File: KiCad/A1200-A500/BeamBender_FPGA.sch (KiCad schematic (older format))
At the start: 1 part, among them U2 GW1NR-UV9LQ144P

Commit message: more routing done
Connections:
- net B0_FPGA: now also U2.40 (IOB9A)
- net B1_FPGA: now also U2.41 (IOB9B)
- net B2_FPGA: now also U2.42 (IOB11A)
- net B3_FPGA: now also U2.43 (IOB11B)
- net B4_FPGA: now also U2.44 (IOB12A)
- net B5_FPGA: now also U2.45 (IOB12B)
- net B6_FPGA: now also U2.46 (IOB13A)
- net B7_FPGA: now also U2.47 (IOB13B)
- net G0_FPGA: now also U2.48 (IOB15A); no longer U2.47 (IOB13B)
- net PCLK: now also U2.34 (IOB6B); no longer U2.48 (IOB15A)
- net VSYNC_FPGA: now reaches U2.32 (IOB6A)
- net HSYNC_FPGA: now reaches U2.38 (IOB8A)
- net DE: now reaches U2.39 (IOB8B)
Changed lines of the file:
@@
 Text GLabel 6500 1800 2    50   Input ~ 0
 GCLKT_1
-Text GLabel 3050 6150 3    50   Output ~ 0
+Text GLabel 1600 5400 0    50   Output ~ 0
 PCLK
 Text GLabel 1600 3000 0    50   Input ~ 0
@@
 Text GLabel 6500 3950 2    50   Input ~ 0
 C14M_3V3
-Text GLabel 8050 4950 2    50   Input ~ 0
+Text GLabel 2250 6150 3    50   Output ~ 0
 B0_FPGA
-Text GLabel 8050 4850 2    50   Input ~ 0
+Text GLabel 2350 6150 3    50   Output ~ 0
 B1_FPGA
-Text GLabel 8050 4750 2    50   Input ~ 0
+Text GLabel 2450 6150 3    50   Output ~ 0
 B2_FPGA
-Text GLabel 8050 4650 2    50   Input ~ 0
+Text GLabel 2550 6150 3    50   Output ~ 0
 B3_FPGA
-Text GLabel 8050 4550 2    50   Input ~ 0
+Text GLabel 2650 6150 3    50   Output ~ 0
 B4_FPGA
-Text GLabel 8050 4450 2    50   Input ~ 0
+Text GLabel 2750 6150 3    50   Output ~ 0
 B5_FPGA
-Text GLabel 8050 4350 2    50   Input ~ 0
+Text GLabel 2850 6150 3    50   Output ~ 0
 B6_FPGA
-Text GLabel 8050 4250 2    50   Input ~ 0
+Text GLabel 2950 6150 3    50   Output ~ 0
 B7_FPGA
-Text GLabel 2950 6150 3    50   Input ~ 0
+Text GLabel 3050 6150 3    50   Output ~ 0
 G0_FPGA
-Text GLabel 3150 6150 3    50   Input ~ 0
+Text GLabel 3150 6150 3    50   Output ~ 0
 G1_FPGA
-Text GLabel 3250 6150 3    50   Input ~ 0
+Text GLabel 3250 6150 3    50   Output ~ 0
 G2_FPGA
-Text GLabel 3350 6150 3    50   Input ~ 0
+Text GLabel 3350 6150 3    50   Output ~ 0
 G3_FPGA
-Text GLabel 3450 6150 3    50   Input ~ 0
+Text GLabel 3450 6150 3    50   Output ~ 0
 G4_FPGA
-Text GLabel 3600 6150 3    50   Input ~ 0
+Text GLabel 3600 6150 3    50   Output ~ 0
 G5_FPGA
-Text GLabel 3750 6150 3    50   Input ~ 0
+Text GLabel 3750 6150 3    50   Output ~ 0
 G6_FPGA
-Text GLabel 3850 6150 3    50   Input ~ 0
+Text GLabel 3850 6150 3    50   Output ~ 0
 G7_FPGA
-Text GLabel 4050 6150 3    50   Input ~ 0
+Text GLabel 4050 6150 3    50   Output ~ 0
 R0_FPGA
-Text GLabel 4150 6150 3    50   Input ~ 0
+Text GLabel 4150 6150 3    50   Output ~ 0
 R1_FPGA
-Text GLabel 4250 6150 3    50   Input ~ 0
+Text GLabel 4250 6150 3    50   Output ~ 0
 R2_FPGA
-Text GLabel 4350 6150 3    50   Input ~ 0
+Text GLabel 4350 6150 3    50   Output ~ 0
 R3_FPGA
-Text GLabel 4450 6150 3    50   Input ~ 0
+Text GLabel 4450 6150 3    50   Output ~ 0
 R4_FPGA
-Text GLabel 4550 6150 3    50   Input ~ 0
+Text GLabel 4550 6150 3    50   Output ~ 0
 R5_FPGA
-Text GLabel 4650 6150 3    50   Input ~ 0
+Text GLabel 4650 6150 3    50   Output ~ 0
 R6_FPGA
-Text GLabel 4750 6150 3    50   Input ~ 0
+Text GLabel 4750 6150 3    50   Output ~ 0
 R7_FPGA
-Text GLabel 5150 6150 3    50   Input ~ 0
-R0_3V3
-Text GLabel 5250 6150 3    50   Input ~ 0
-R1_3V3
-Text GLabel 5350 6150 3    50   Input ~ 0
-R2_3V3
-Text GLabel 5450 6150 3    50   Input ~ 0
-R3_3V3
 Text GLabel 6500 4650 2    50   Input ~ 0
 B0_3V3
@@
 Text GLabel 6500 4850 2    50   Input ~ 0
 G7_3V3
-Text GLabel 5550 6150 3    50   Input ~ 0
-R4_3V3
-Text GLabel 5650 6150 3    50   Input ~ 0
-R5_3V3
-Text GLabel 6500 5750 2    50   Input ~ 0
-R6_3V3
 Text GLabel 6500 5650 2    50   Input ~ 0
 R7_3V3
 Text GLabel 3950 6150 3    50   Input ~ 0
 XTAL_27M
-Text GLabel 4950 6150 3    50   Input ~ 0
+Text GLabel 4950 6150 3    50   Output ~ 0
 SCL_I2C
 Text GLabel 4850 6150 3    50   BiDi ~ 0
@@
 Text GLabel 5050 6150 3    50   Input ~ 0
 INT
+Text GLabel 2150 6150 3    50   Output ~ 0
+DE
+Text GLabel 1600 5250 0    50   Output ~ 0
+VSYNC_FPGA
+Text GLabel 2050 6150 3    50   Output ~ 0
+HSYNC_FPGA
+Text GLabel 6500 5750 2    50   Input ~ 0
+R6_3V3
+Text GLabel 5650 6150 3    50   Input ~ 0
+R5_3V3
+Text GLabel 5550 6150 3    50   Input ~ 0
+R4_3V3
+Text GLabel 5450 6150 3    50   Input ~ 0
+R3_3V3
+Text GLabel 5350 6150 3    50   Input ~ 0
+R2_3V3
+Text GLabel 5250 6150 3    50   Input ~ 0
+R1_3V3
+Text GLabel 5150 6150 3    50   Input ~ 0
+R0_3V3
 $EndSCHEMATC

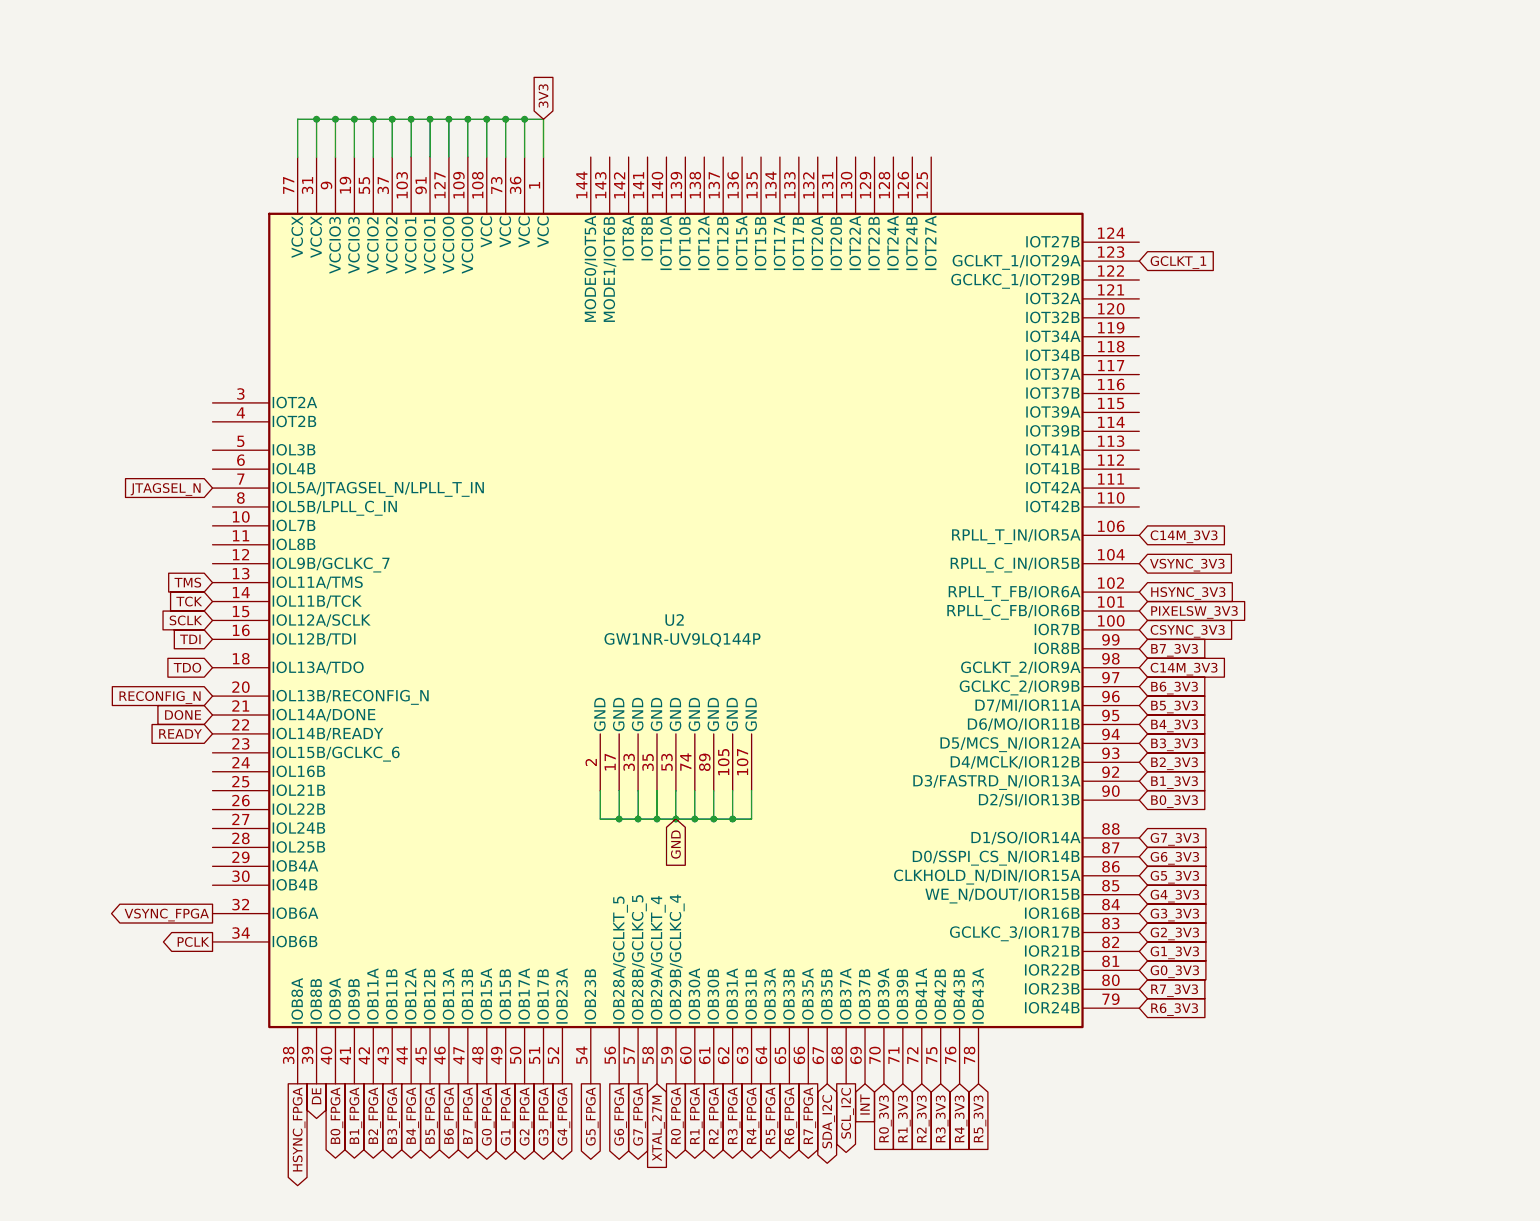
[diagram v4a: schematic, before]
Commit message: Added Oscillator_7.0x5.0mm X2 on GCLKT_1 input and added damping resistor on PCLK
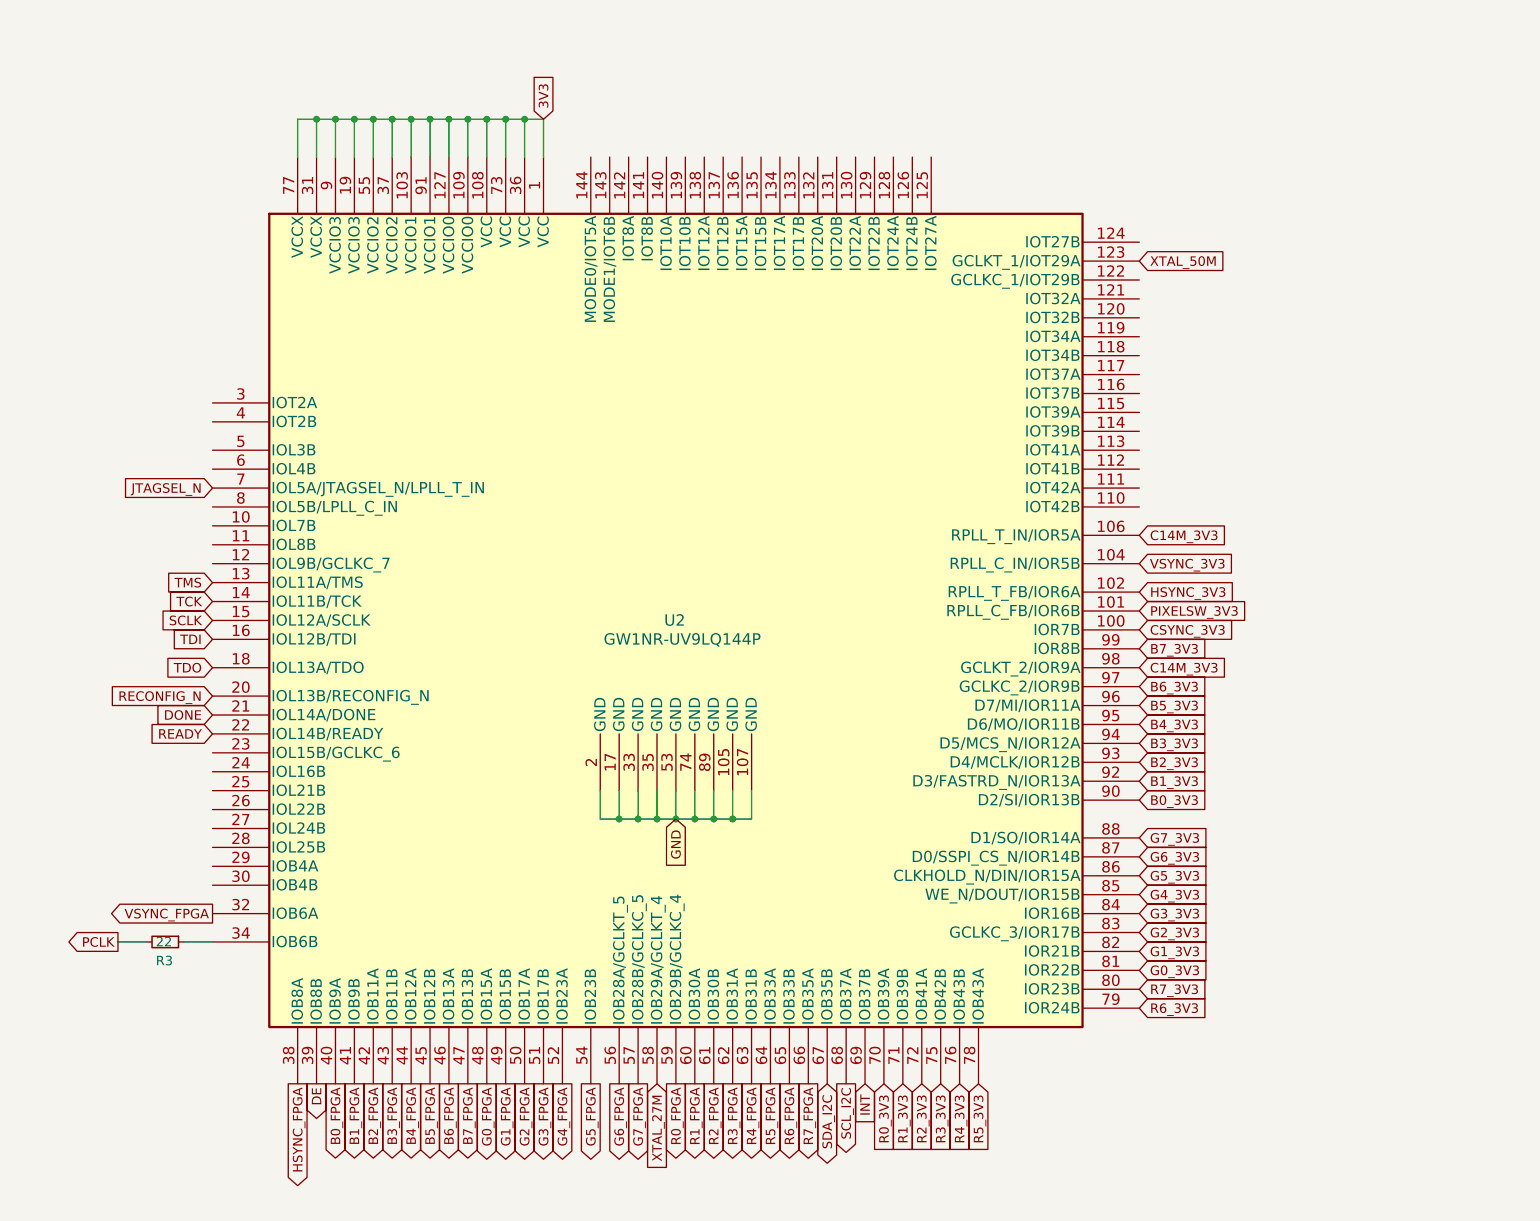
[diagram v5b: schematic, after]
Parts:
- added R3: 22, Resistor_SMD:R_0603_1608Metric_Pad0.98x0.95mm_HandSolder, symbol Device:R_Small
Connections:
- net PCLK: now also R3.2; no longer U2.34 (IOB6B)
- net GCLKT_1 renamed XTAL_50M
- new net: R3.1, U2.34 (IOB6B)
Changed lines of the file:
@@
 Text GLabel 1600 4300 0    50   Input ~ 0
 READY
-Text GLabel 6500 1800 2    50   Input ~ 0
-GCLKT_1
-Text GLabel 1600 5400 0    50   Output ~ 0
+Text GLabel 1100 5400 0    50   Output ~ 0
 PCLK
 Text GLabel 1600 3000 0    50   Input ~ 0
@@
 Text GLabel 5150 6150 3    50   Input ~ 0
 R0_3V3
+Text GLabel 6500 1800 2    50   Input ~ 0
+XTAL_50M
+$Comp
+L Device:R_Small R?
+U 1 1 65968AC9
+P 1350 5400
+AR Path="/65968AC9" Ref="R?"  Part="1"
+AR Path="/6541C824/65968AC9" Ref="R3"  Part="1"
+F 0 "R3" V 1450 5350 50  0000 L CNN
+F 1 "22" V 1350 5350 50  0000 L CNN
+F 2 "Resistor_SMD:R_0603_1608Metric_Pad0.98x0.95mm_HandSolder" H 1350 5400 50  0001 C CNN
+F 3 "~" H 1350 5400 50  0001 C CNN
+	1    1350 5400
+	0    1    1    0
+$EndComp
+Wire Wire Line
+	1600 5400 1450 5400
+Wire Wire Line
+	1250 5400 1100 5400
 $EndSCHEMATC

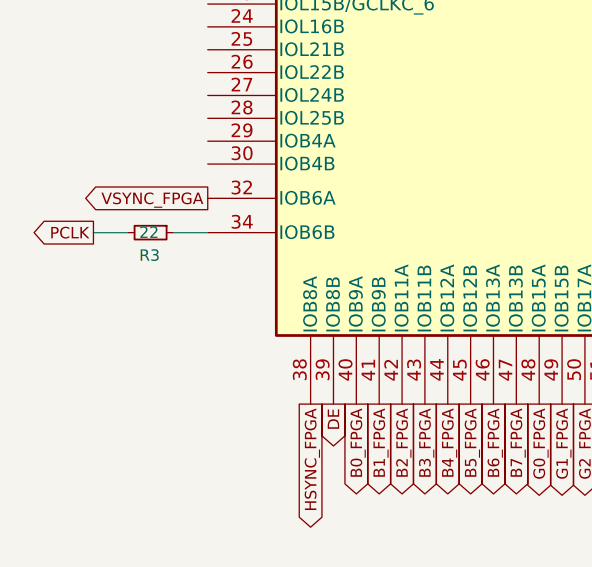
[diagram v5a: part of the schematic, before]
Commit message: Added a 1.8V LDO (MCP1702T-1802E_CB) in SOT-23 for powering the ADV7513 with 1.8V (DVDD,AVDD,PVDD,BGVDD)
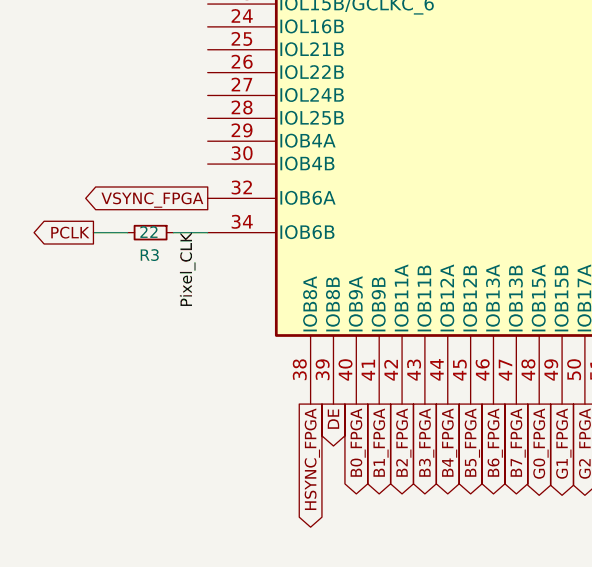
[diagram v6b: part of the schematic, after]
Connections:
- net Pixel_CLK: now reaches R3.1, U2.34 (IOB6B)
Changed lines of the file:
@@
 Wire Wire Line
 	1250 5400 1100 5400
+Text Label 1550 5400 3    50   ~ 0
+Pixel_CLK
 $EndSCHEMATC
